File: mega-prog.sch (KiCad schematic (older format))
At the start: 29 parts, among them P1 USB_B, P2 MD-CART-PORT, P3 CONN_02X03, SW1 SW_PUSH, U1 AT90USB646, U2 74LVC2G14, Y1 8MHz, Y2 14.74MHz

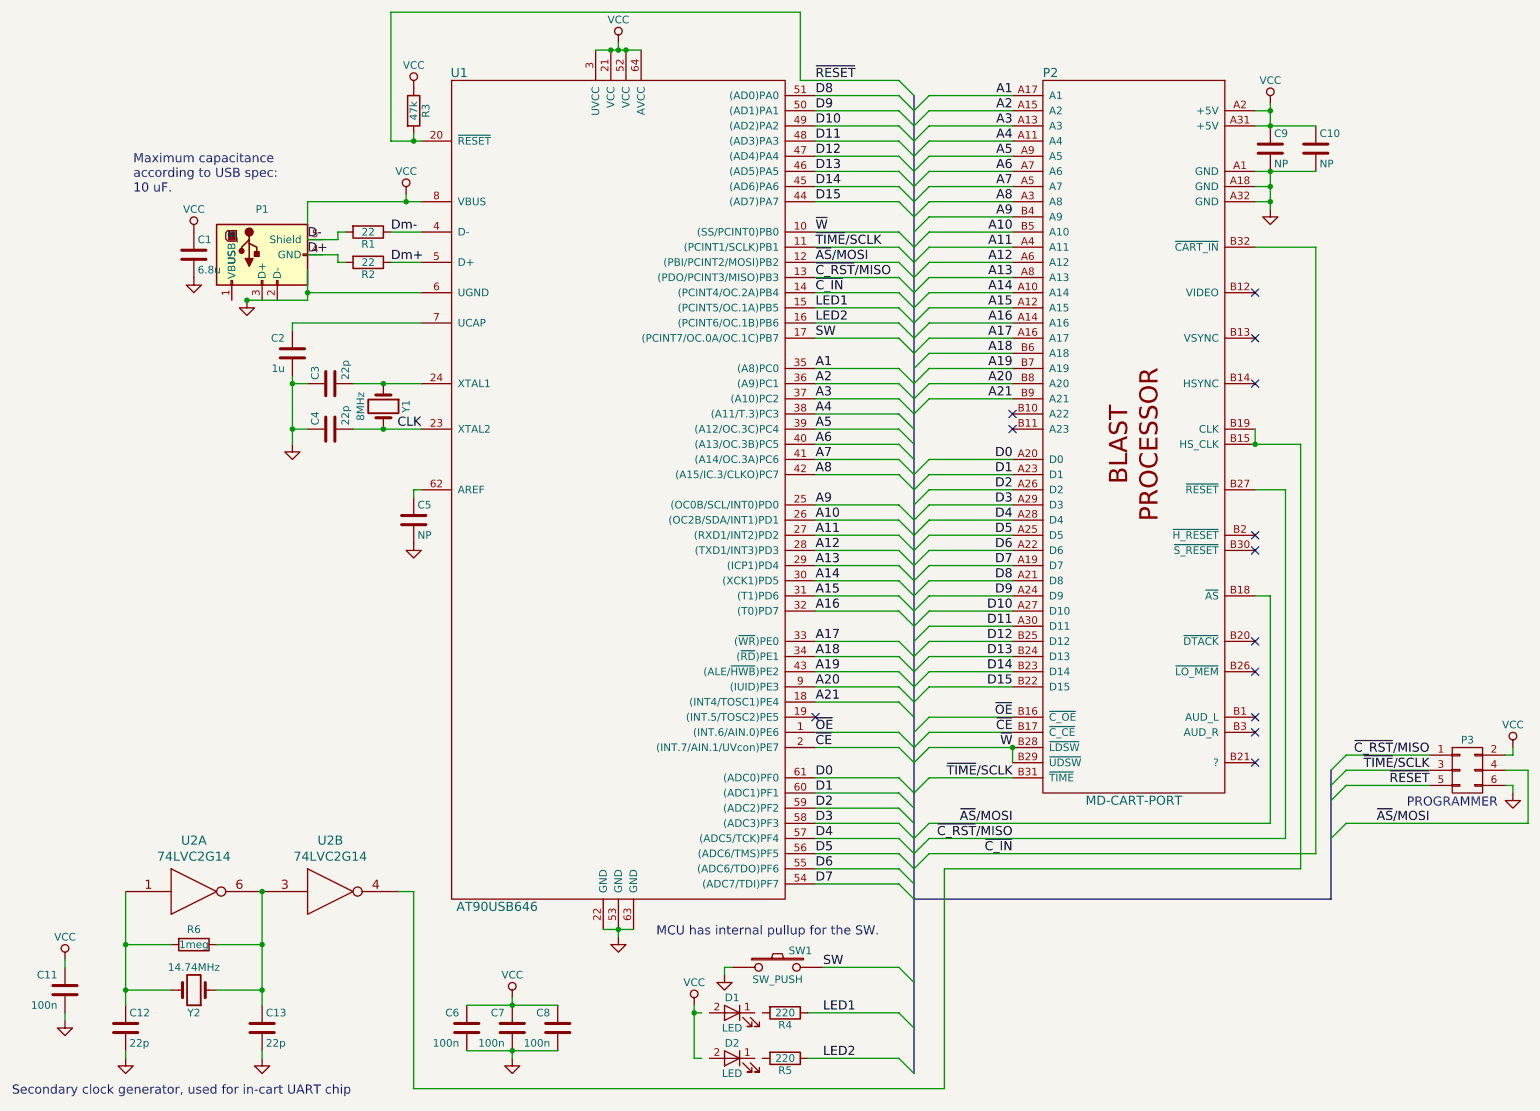
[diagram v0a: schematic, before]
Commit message: BOM changes.
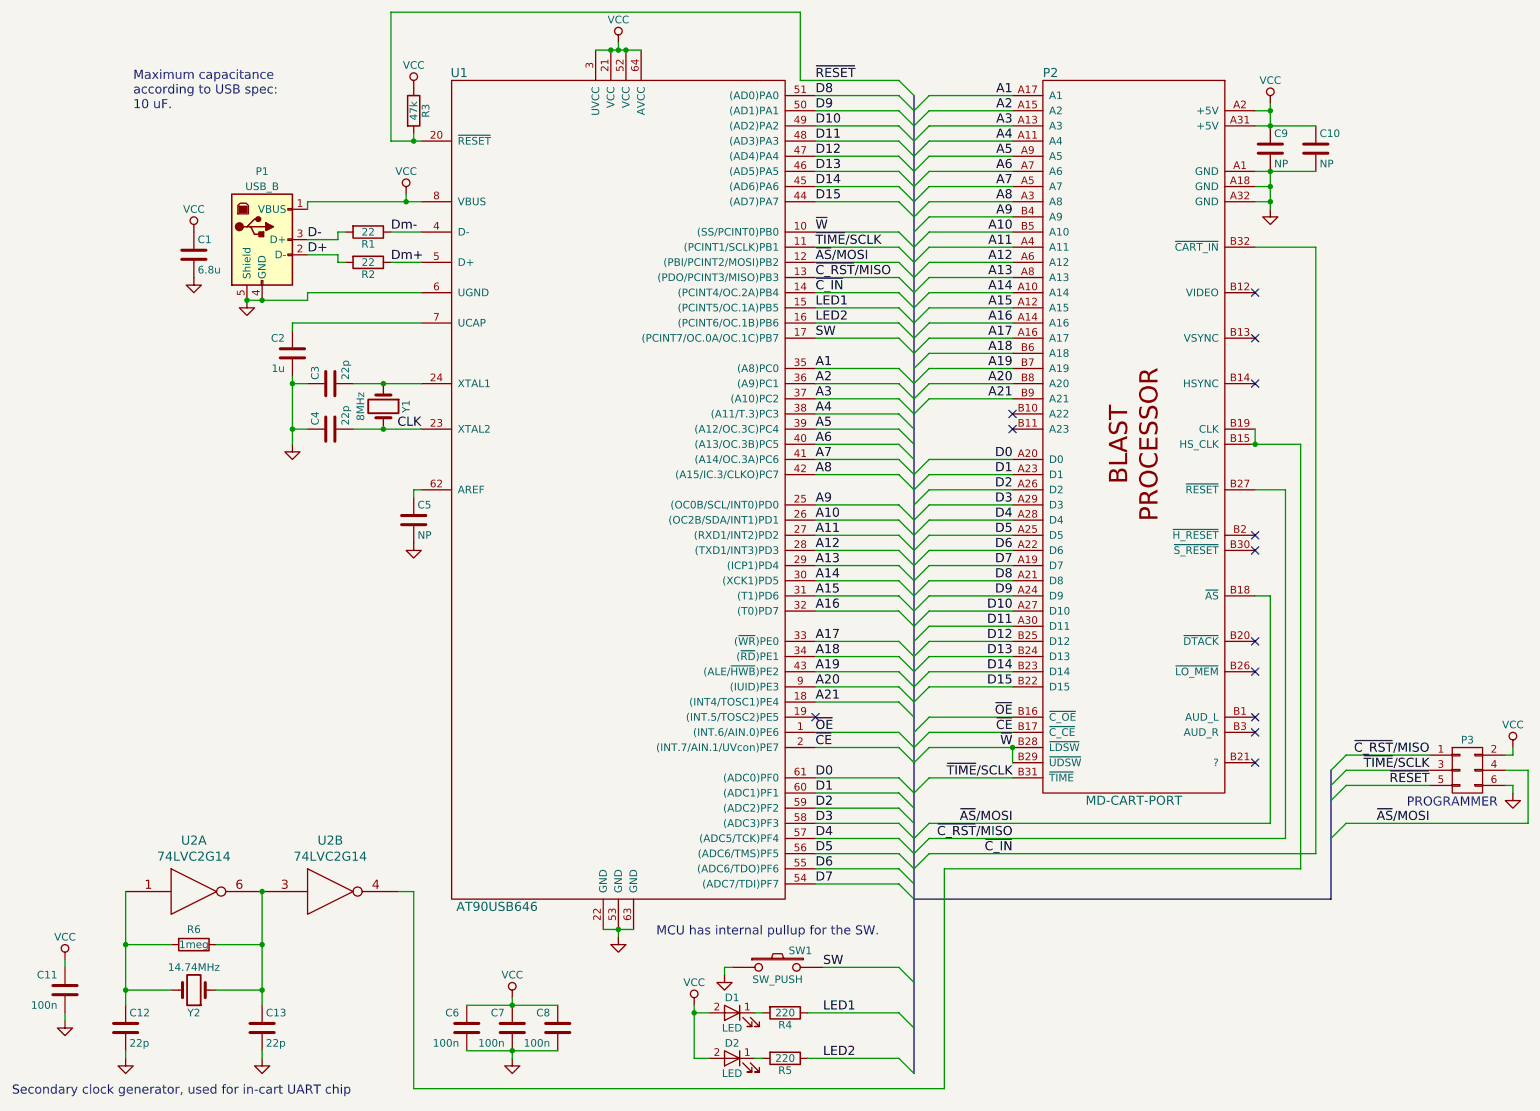
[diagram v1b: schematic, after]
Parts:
- C1: manf# (none) -> 865080440001
- C11: manf# (none) -> CL21B104MBCNNNC
- C2: manf# (none) -> CL21B105KOFNNNG
- C3: manf# (none) -> CL10C220JB8NNWC
- D1: manf# (none) -> LTL2R3KRD-EM
- D2: manf# (none) -> LTL2R3KGD-EM
- P1: manf# (none) -> E8144-B02022-L
- P2: manf# (none) -> 1761469-1
- P3: manf# (none) -> M20-9760346
- R1: manf# (none) -> RMCF0805JT22R0CT-ND
- R3: manf# (none) -> RMCF0805JT47K0
- R4: manf# (none) -> RMCF0805JT220R
- SW1: manf# (none) -> 3-1825910-1
- U1: manf# (none) -> AT90USB646-AUR
- Y1: manf# (none) -> ABL-8.000MHZ-B2
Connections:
- net D+: now also P1.2 (D-)
- net D-: now also P1.3 (D+)
- net GND: now also P1.4 (GND), P1.5 (Shield)
- net VCC: now also D1.2 (A), D2.2 (A), P1.1 (VBUS)
- net at D2.1 (K): now also R5.2
- net at D1.1 (K): now also R4.2
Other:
- moved on the sheet: P1
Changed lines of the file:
@@
 L USB_B P1
 U 1 1 562297B1
-P 2150 2150
-F 0 "P1" V 1850 2150 50  0000 C CNN
-F 1 "USB_B" H 2100 2350 50  0000 C CNN
-F 2 "Connect:USB_B" V 2100 2050 60  0001 C CNN
-F 3 "" V 2100 2050 60  0000 C CNN
-	1    2150 2150
-	0    -1   1    0
+P 2150 2050
+F 0 "P1" H 2150 2500 50  0000 C CNN
+F 1 "USB_B" H 2150 2400 50  0000 C CNN
+F 2 "Connect:USB_B" V 2100 1950 60  0001 C CNN
+F 3 "" V 2100 1950 60  0000 C CNN
+F 4 "E8144-B02022-L" H 2150 2050 60  0001 C CNN "manf#"
+	1    2150 2050
+	1    0    0    -1
 $EndComp
 $Comp
@@
 F 2 "Housings_QFP:LQFP-64_14x14mm_Pitch0.8mm" H 3850 2750 60  0001 C CNN
 F 3 "" H 3850 2750 60  0000 C CNN
+F 4 "AT90USB646-AUR" H 4500 3700 60  0001 C CNN "manf#"
 	1    4500 3700
 	1    0    0    -1
@@
 F 2 "Resistors_SMD:R_0805" V 3080 1200 30  0001 C CNN
 F 3 "" H 3150 1200 30  0000 C CNN
+F 4 "RMCF0805JT47K0" V 3150 1200 60  0001 C CNN "manf#"
 	1    3150 1200
 	1    0    0    -1
@@
 F 2 "Crystals:Crystal_HC49-U_Vertical" H 2950 3150 60  0001 C CNN
 F 3 "" H 2950 3150 60  0000 C CNN
+F 4 "ABL-8.000MHZ-B2" H 2950 3150 60  0001 C CNN "manf#"
 	1    2950 3150
 	0    1    1    0
@@
 F 2 "Capacitors_SMD:C_0805" H 2638 2850 30  0001 C CNN
 F 3 "" H 2600 3000 60  0000 C CNN
+F 4 "CL10C220JB8NNWC" H 2600 3000 60  0001 C CNN "manf#"
 	1    2600 3000
 	0    -1   -1   0
@@
 F 2 "Capacitors_SMD:C_0805" H 2388 2650 30  0001 C CNN
 F 3 "" H 2350 2800 60  0000 C CNN
+F 4 "CL21B105KOFNNNG" H 2350 2800 60  0001 C CNN "manf#"
 	1    2350 2800
 	1    0    0    -1
@@
 F 2 "Capacitors_ThroughHole:Capacitor5x11RM2.5" H 1738 2000 30  0001 C CNN
 F 3 "" H 1700 2150 60  0000 C CNN
+F 4 "865080440001" H 1700 2150 60  0001 C CNN "manf#"
 	1    1700 2150
 	1    0    0    -1
@@
 F 2 "LEDs:LED-5MM" H 5250 7450 60  0001 C CNN
 F 3 "" H 5250 7450 60  0000 C CNN
+F 4 "LTL2R3KGD-EM" H 5250 7450 60  0001 C CNN "manf#"
 	1    5250 7450
 	-1   0    0    -1
@@
 F 2 "LEDs:LED-5MM" H 5250 7150 60  0001 C CNN
 F 3 "" H 5250 7150 60  0000 C CNN
+F 4 "LTL2R3KRD-EM" H 5250 7150 60  0001 C CNN "manf#"
 	1    5250 7150
 	-1   0    0    -1
@@
 F 2 "Discret:SW_PUSH_SMALL" H 5550 6850 60  0001 C CNN
 F 3 "" H 5550 6850 60  0000 C CNN
+F 4 "3-1825910-1" H 5550 6850 60  0001 C CNN "manf#"
 	1    5550 6850
 	1    0    0    -1
@@
 F 2 "Resistors_SMD:R_0805" V 5530 7150 30  0001 C CNN
 F 3 "" H 5600 7150 30  0000 C CNN
+F 4 "RMCF0805JT220R" V 5600 7150 60  0001 C CNN "manf#"
 	1    5600 7150
 	0    1    1    0
@@
 F 2 "Resistors_SMD:R_0805" V 2780 2000 30  0001 C CNN
 F 3 "" H 2850 2000 30  0000 C CNN
+F 4 "RMCF0805JT22R0CT-ND" V 2850 2000 60  0001 C CNN "manf#"
 	1    2850 2000
 	0    1    1    0
@@
 Text Notes 4750 6650 0    60   ~ 0
 MCU has internal pullup for the SW.
-Text Notes 1300 1750 0    60   ~ 0
+Text Notes 1300 1200 0    60   ~ 0
 Maximum capacitance\naccording to USB spec:\n10 uF.
 $Comp
@@
 F 2 "doragasu:GEN_CART_PORT" H 8350 2700 60  0001 C CNN
 F 3 "" H 8350 2700 60  0000 C CNN
+F 4 "1761469-1" H 7900 3400 60  0001 C CNN "manf#"
 	1    7900 3400
 	1    0    0    -1
@@
 F 2 "Pin_Headers:Pin_Header_Straight_2x03" H 10100 4350 60  0001 C CNN
 F 3 "" H 10100 4350 60  0000 C CNN
+F 4 "M20-9760346" H 10100 5550 60  0001 C CNN "manf#"
 	1    10100 5550
 	1    0    0    -1
@@
 F 2 "Capacitors_SMD:C_0805" H 888 6850 30  0001 C CNN
 F 3 "" H 850 7000 60  0000 C CNN
+F 4 "CL21B104MBCNNNC" H 850 7000 60  0001 C CNN "manf#"
 	1    850  7000
 	1    0    0    -1
@@
 	6450 1100 6450 7550
 Wire Wire Line
-	5000 7450 5050 7450
+	5000 7450 5100 7450
 Connection ~ 5000 7150
 Wire Wire Line
@@
 	3000 2200 3200 2200
 Wire Wire Line
-	2450 2250 2450 2450
-Wire Wire Line
 	3200 2400 2450 2400
-Connection ~ 2450 2400
-Wire Wire Line
-	2450 1950 2450 1800
 Wire Wire Line
 	2650 2150 2650 2200
@@
 	5000 7100 5000 7450
 Wire Wire Line
-	5000 7150 5050 7150
+	5000 7150 5100 7150
 Wire Wire Line
 	5800 2500 6350 2500
@@
 Text Notes 500  7700 0    60   ~ 0
 Secondary clock generator, used for in-cart UART chip
+Wire Wire Line
+	5400 7150 5450 7150
+Wire Wire Line
+	5400 7450 5450 7450
+Wire Wire Line
+	2450 1800 2450 1850
+Wire Wire Line
+	2450 2400 2450 2450
+Connection ~ 2150 2450
 $EndSCHEMATC

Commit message: Updated to latest KiCad and libraries version.
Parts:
- removed P1: USB_B, Connect:USB_B, symbol USB_B
- removed P3: CONN_02X03, Pin_Headers:Pin_Header_Straight_2x03, symbol CONN_02X03
- removed SW1: SW_PUSH, Discret:SW_PUSH_SMALL, symbol SW_PUSH
- added J?: Conn_02x03_Odd_Even, Pin_Headers:Pin_Header_Straight_2x03, symbol Connector:Conn_02x03_Odd_Even
- added P1: USB_B, Connect:USB_B, symbol Connector:USB_B
- added SW1: SW_Push, Discret:SW_PUSH_SMALL, symbol Switch:SW_Push
- C1, C10, C11, C12, C13, C2, C3, C4, C5, C6, C7, C8, C9: symbol C -> device:C
- D1, D2: symbol LED -> device:LED
- P2: symbol MD-CART-PORT -> doragasu:MD-CART-PORT
- R1, R2, R3, R4, R5, R6: symbol R -> device:R
- U1: symbol AT90USB646 -> doragasu:AT90USB646
- U2: symbol 74LVC2G14 -> doragasu:74LVC2G14
- Y1, Y2: symbol Crystal -> device:Crystal
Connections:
- net D+: now also P1.3 (D+)
- net D-: now also P1.2 (D-)
- net GND: now also J?.6 (Pin_6), P1.4 (GND), P1.5 (Shield), SW1.1
- net SW: now also SW1.2
- net VCC: now also J?.2 (Pin_2), P1.1 (VBUS)
- net ~AS~/MOSI: now also J?.4 (Pin_4)
- net ~C_RST~/MISO: now also J?.1 (Pin_1)
- net ~RESET: now also J?.5 (Pin_5)
- net ~TIME~/SCLK: now also J?.3 (Pin_3)
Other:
- note added: "Secondary clock generator. Currently unused."
- note removed: "Secondary clock generator, used for in-cart UART chip"
- moved on the sheet: C1
